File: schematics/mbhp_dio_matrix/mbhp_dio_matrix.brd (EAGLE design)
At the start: 80 x 40 mm, 22 parts, among them IC1 74HC595, IC2 74HC595, IC3 74HC165, IC4 74HC165

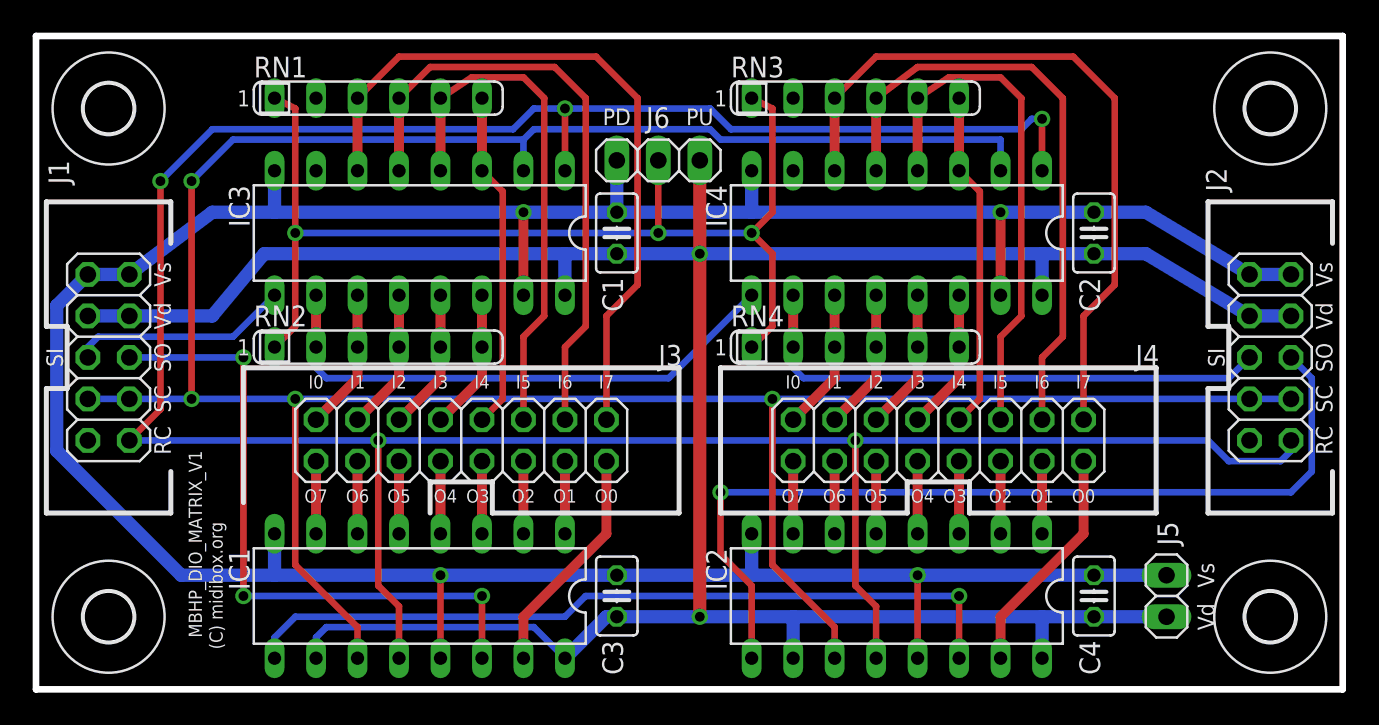
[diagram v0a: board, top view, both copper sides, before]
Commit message: mbhp_dio_matrix: some minor improvements
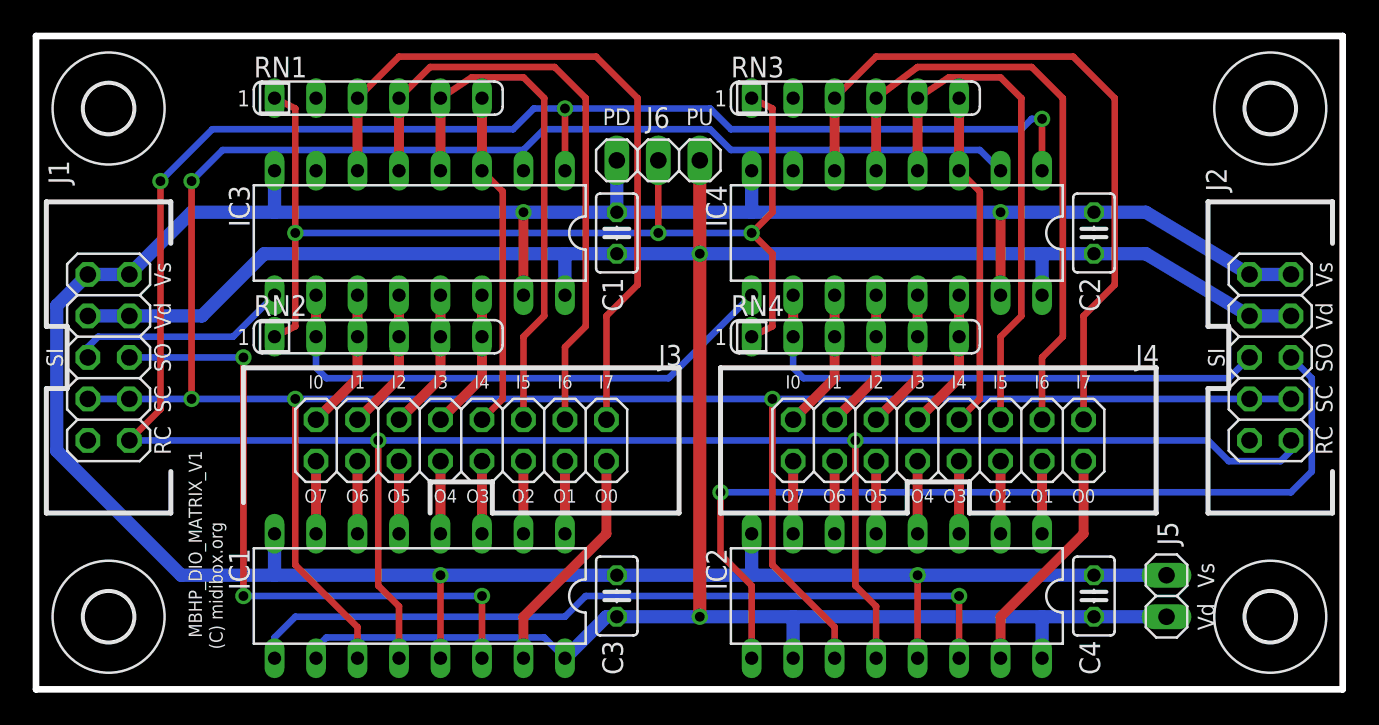
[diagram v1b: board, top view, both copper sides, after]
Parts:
- moved RN2 0.64 mm to (21.0, 21.6)
- moved RN4 0.64 mm to (50.2, 21.6)
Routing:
- net SC: track 176.8 -> 175.1 mm
- net VDD: track 170.0 -> 168.9 mm
- net S$1: track 66.5 -> 65.8 mm
